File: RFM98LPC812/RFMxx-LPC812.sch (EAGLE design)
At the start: 43 parts, among them P14 TPB1,27, X1 BU-SMA-V, X2 BU-SMA-V

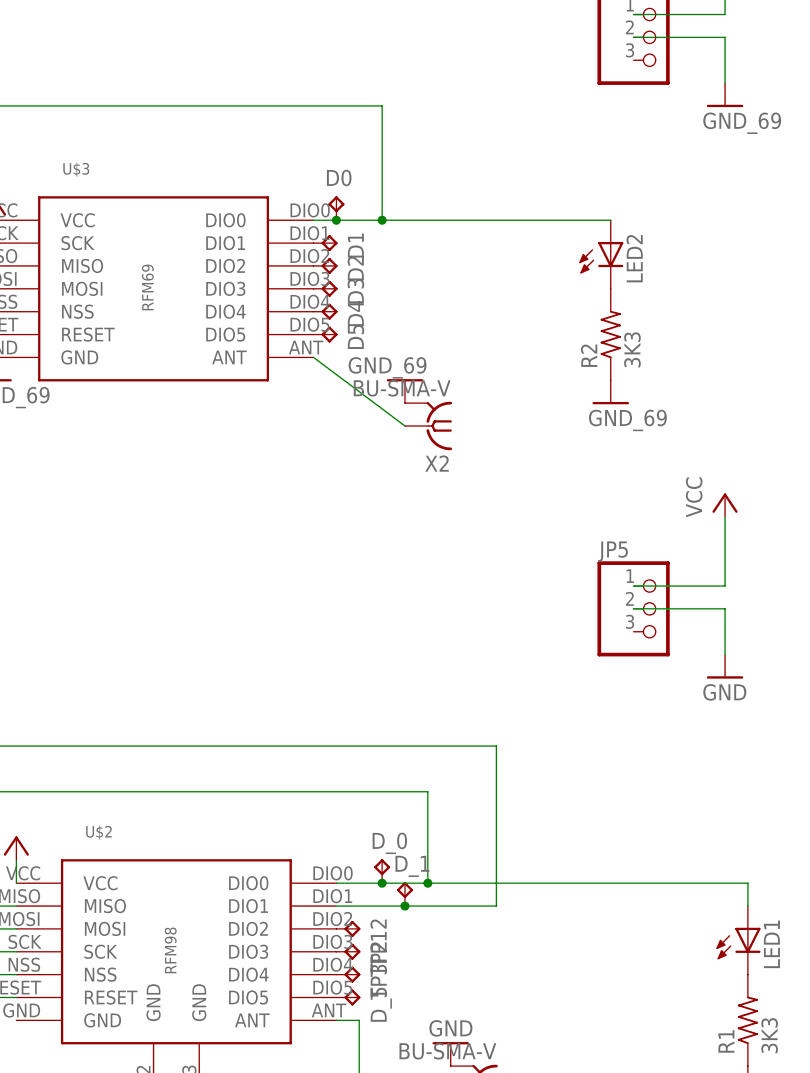
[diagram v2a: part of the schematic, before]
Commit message: Removed TPs, now quote back down to the EUR 85 level.
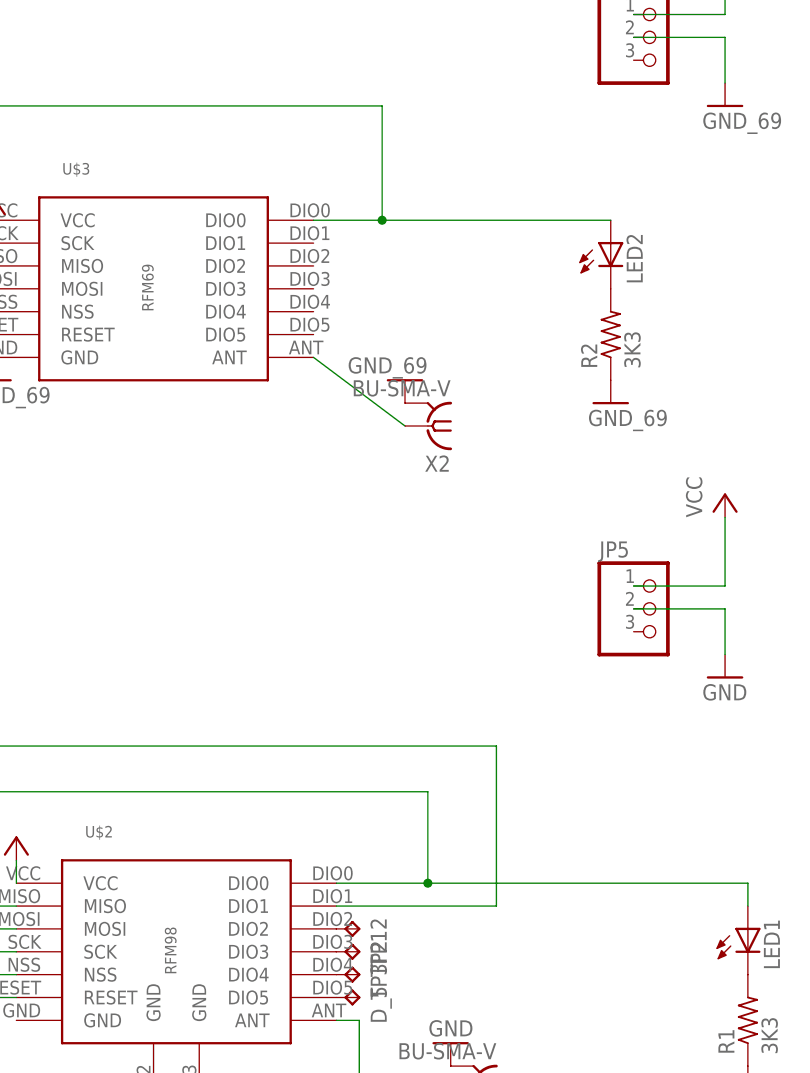
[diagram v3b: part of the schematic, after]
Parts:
- removed D0, D1, D2, D3, D4, D5, D_0, D_1: TPB1,27, testpad:TPB1,27
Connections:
- removed net N$47: D1.TP, U$3.DIO1
- removed net N$48: D2.TP, U$3.DIO2
- removed net N$49: D3.TP, U$3.DIO3
- removed net N$50: D4.TP, U$3.DIO4
- removed net N$51: D5.TP, U$3.DIO5
- net N$22: no longer D_0.TP
- net N$24: no longer D0.TP
- net N$27: no longer D_1.TP
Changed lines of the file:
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@@
 <part name="TP8" library="testpad" deviceset="TP" device="B1,27"/>
 <part name="TP9" library="testpad" deviceset="TP" device="B1,27"/>
-<part name="D1" library="testpad" deviceset="TP" device="B1,27"/>
-<part name="D2" library="testpad" deviceset="TP" device="B1,27"/>
-<part name="D3" library="testpad" deviceset="TP" device="B1,27"/>
-<part name="D4" library="testpad" deviceset="TP" device="B1,27"/>
-<part name="D5" library="testpad" deviceset="TP" device="B1,27"/>
-<part name="D0" library="testpad" deviceset="TP" device="B1,27"/>
-<part name="D_0" library="testpad" deviceset="TP" device="B1,27"/>
-<part name="D_1" library="testpad" deviceset="TP" device="B1,27"/>
 <part name="TP12" library="testpad" deviceset="TP" device="B1,27"/>
 <part name="P+1" library="supply1" deviceset="VCC" device=""/>
@@
 <instance part="TP8" gate="G$1" x="-121.92" y="38.1" rot="R90"/>
 <instance part="TP9" gate="G$1" x="-121.92" y="35.56" rot="R90"/>
-<instance part="D1" gate="G$1" x="20.32" y="45.72" rot="R270"/>
-<instance part="D2" gate="G$1" x="20.32" y="43.18" rot="R270"/>
-<instance part="D3" gate="G$1" x="20.32" y="40.64" rot="R270"/>
-<instance part="D4" gate="G$1" x="20.32" y="38.1" rot="R270"/>
-<instance part="D5" gate="G$1" x="20.32" y="35.56" rot="R270"/>
-<instance part="D0" gate="G$1" x="20.32" y="50.8"/>
-<instance part="D_0" gate="G$1" x="25.4" y="-22.86"/>
-<instance part="D_1" gate="G$1" x="27.94" y="-25.4"/>
 <instance part="TP12" gate="G$1" x="22.86" y="-30.48" rot="R270"/>
 <instance part="P+1" gate="VCC" x="-93.98" y="2.54"/>
@@
 <wire x1="30.48" y1="-15.24" x2="30.48" y2="-25.4" width="0.1524" layer="91"/>
 <pinref part="U$2" gate="G$1" pin="DIO0"/>
-<wire x1="30.48" y1="-25.4" x2="25.4" y2="-25.4" width="0.1524" layer="91"/>
-<wire x1="25.4" y1="-25.4" x2="20.32" y2="-25.4" width="0.1524" layer="91"/>
+<wire x1="30.48" y1="-25.4" x2="20.32" y2="-25.4" width="0.1524" layer="91"/>
 <wire x1="-33.02" y1="-15.24" x2="-33.02" y2="-25.4" width="0.1524" layer="91"/>
 <pinref part="JP4" gate="A" pin="1"/>
@@
 <wire x1="66.04" y1="-25.4" x2="66.04" y2="-27.94" width="0.1524" layer="91"/>
 <junction x="30.48" y="-25.4"/>
-<pinref part="D_0" gate="G$1" pin="TP"/>
-<junction x="25.4" y="-25.4"/>
 </segment>
 </net>
@@
 <wire x1="38.1" y1="-10.16" x2="38.1" y2="-27.94" width="0.1524" layer="91"/>
 <pinref part="U$2" gate="G$1" pin="DIO1"/>
-<wire x1="38.1" y1="-27.94" x2="27.94" y2="-27.94" width="0.1524" layer="91"/>
-<pinref part="D_1" gate="G$1" pin="TP"/>
-<wire x1="27.94" y1="-27.94" x2="20.32" y2="-27.94" width="0.1524" layer="91"/>
-<junction x="27.94" y="-27.94"/>
+<wire x1="38.1" y1="-27.94" x2="20.32" y2="-27.94" width="0.1524" layer="91"/>
 </segment>
 </net>
@@
 <segment>
 <pinref part="U$3" gate="G$1" pin="DIO0"/>
-<wire x1="17.78" y1="48.26" x2="20.32" y2="48.26" width="0.1524" layer="91"/>
-<wire x1="20.32" y1="48.26" x2="25.4" y2="48.26" width="0.1524" layer="91"/>
+<wire x1="17.78" y1="48.26" x2="25.4" y2="48.26" width="0.1524" layer="91"/>
 <wire x1="25.4" y1="48.26" x2="25.4" y2="60.96" width="0.1524" layer="91"/>
 <wire x1="25.4" y1="60.96" x2="-53.34" y2="60.96" width="0.1524" layer="91"/>
@@
 <wire x1="25.4" y1="48.26" x2="50.8" y2="48.26" width="0.1524" layer="91"/>
 <junction x="25.4" y="48.26"/>
-<pinref part="D0" gate="G$1" pin="TP"/>
-<junction x="20.32" y="48.26"/>
 </segment>
 </net>
@@
 </segment>
 </net>
-<net name="N$47" class="0">
-<segment>
-<pinref part="U$3" gate="G$1" pin="DIO1"/>
-<pinref part="D1" gate="G$1" pin="TP"/>
-</segment>
-</net>
-<net name="N$48" class="0">
-<segment>
-<pinref part="U$3" gate="G$1" pin="DIO2"/>
-<pinref part="D2" gate="G$1" pin="TP"/>
-</segment>
-</net>
-<net name="N$49" class="0">
-<segment>
-<pinref part="U$3" gate="G$1" pin="DIO3"/>
-<pinref part="D3" gate="G$1" pin="TP"/>
-</segment>
-</net>
-<net name="N$50" class="0">
-<segment>
-<pinref part="U$3" gate="G$1" pin="DIO4"/>
-<pinref part="D4" gate="G$1" pin="TP"/>
-</segment>
-</net>
-<net name="N$51" class="0">
-<segment>
-<pinref part="U$3" gate="G$1" pin="DIO5"/>
-<pinref part="D5" gate="G$1" pin="TP"/>
-</segment>
-</net>

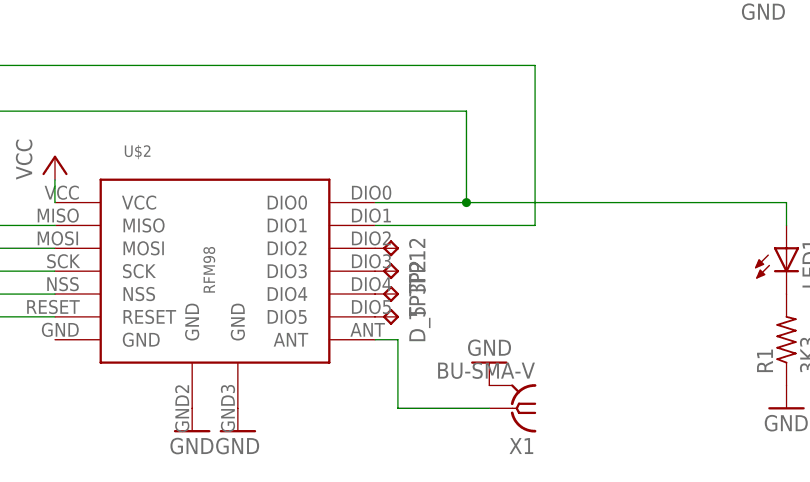
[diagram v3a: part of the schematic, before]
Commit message: fix some clearance issues which is pushing up the price due to using thinner copper foil
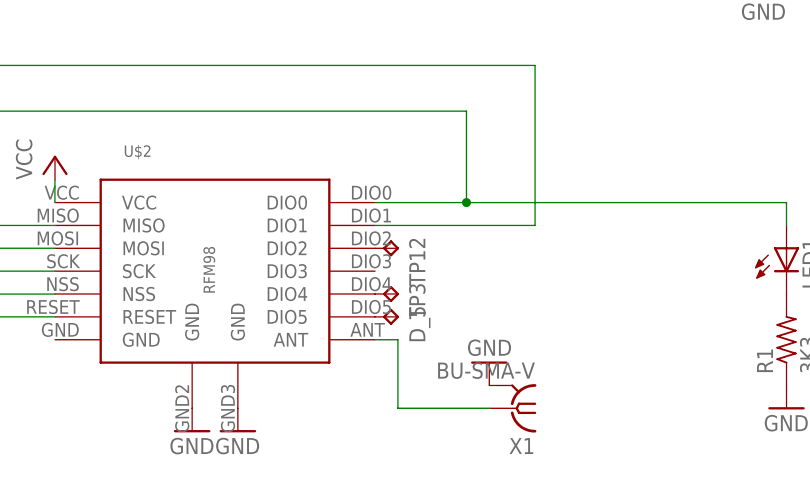
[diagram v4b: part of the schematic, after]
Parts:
- removed TP2: TPB1,27, testpad:TPB1,27
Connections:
- removed net N$30: TP2.TP, U$2.DIO3
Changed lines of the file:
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@@
 <part name="TP1" library="testpad" deviceset="TP" device="B1,27"/>
 <part name="JP7" library="adafruit" deviceset="PINHD-1X3" device=""/>
-<part name="TP2" library="testpad" deviceset="TP" device="B1,27"/>
 <part name="TP3" library="testpad" deviceset="TP" device="B1,27"/>
 <part name="TP4" library="testpad" deviceset="TP" device="B1,27"/>
@@
 <instance part="TP1" gate="G$1" x="-121.92" y="-38.1" rot="R90"/>
 <instance part="JP7" gate="A" x="-137.16" y="-30.48"/>
-<instance part="TP2" gate="G$1" x="22.86" y="-33.02" rot="R270"/>
 <instance part="TP3" gate="G$1" x="22.86" y="-35.56" rot="R270"/>
 <instance part="TP4" gate="G$1" x="-121.92" y="-35.56" rot="R90"/>
@@
 </segment>
 </net>
-<net name="N$30" class="0">
-<segment>
-<pinref part="U$2" gate="G$1" pin="DIO3"/>
-<pinref part="TP2" gate="G$1" pin="TP"/>
-</segment>
-</net>

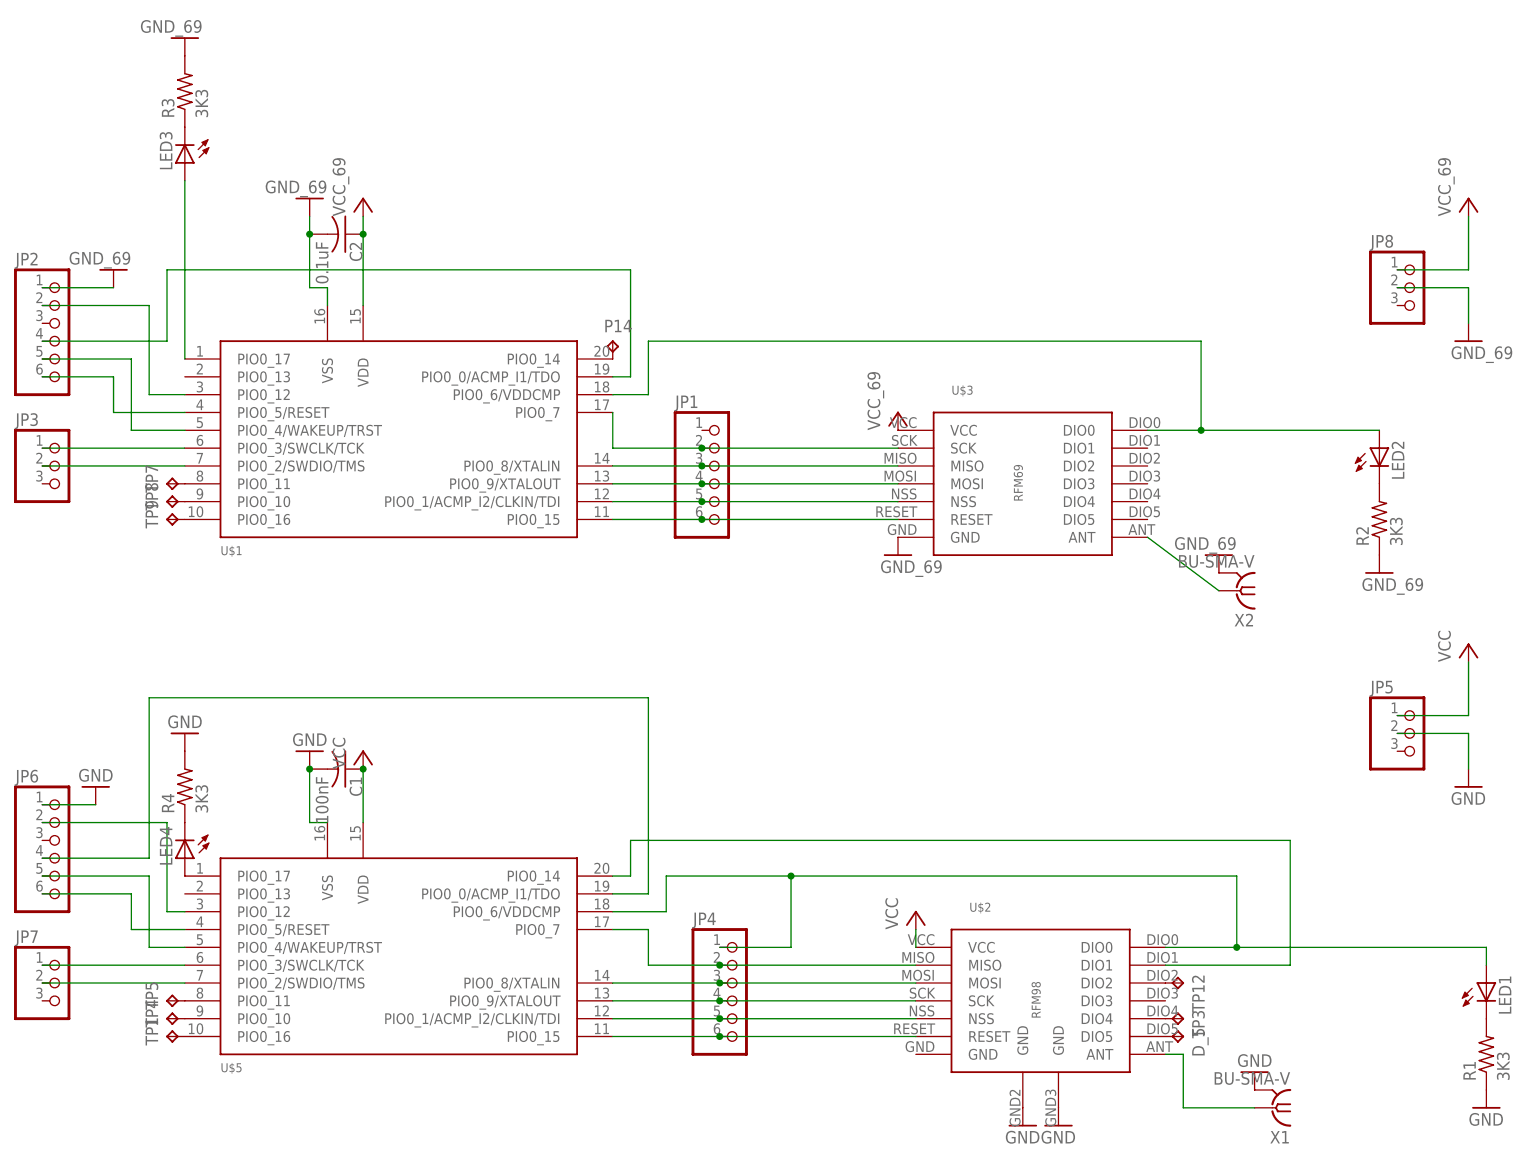
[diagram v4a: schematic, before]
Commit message: label cosmetic changes
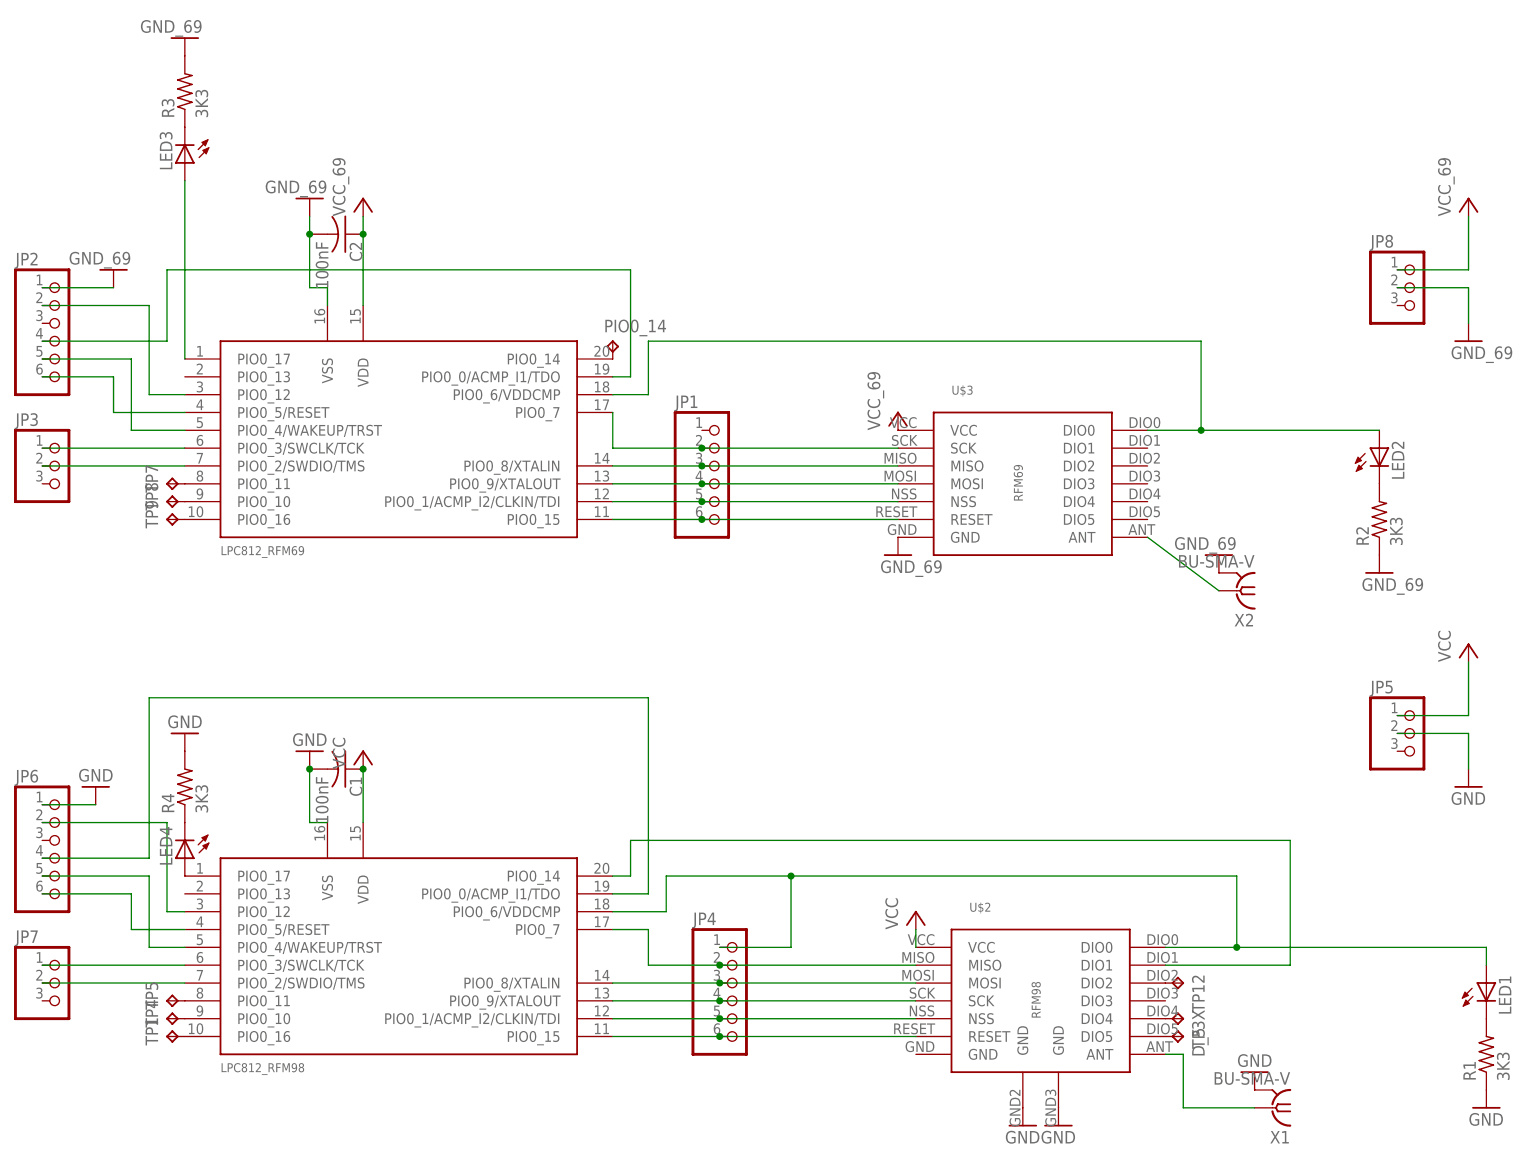
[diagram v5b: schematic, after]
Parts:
- C2: value 0.1uF -> 100nF
- renumbered P14 to PIO0_14, TP3 to TP3X, U$1 to LPC812_RFM69, U$5 to LPC812_RFM98
